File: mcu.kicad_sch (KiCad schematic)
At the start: 13 parts, among them J4 Conn_01x04, SW1 EVQ-P7A01P, SW2 EVQ-P7A01P, U2 TXB0304RUTR, U9 ESP32-S3-WROOM-1-N16R8

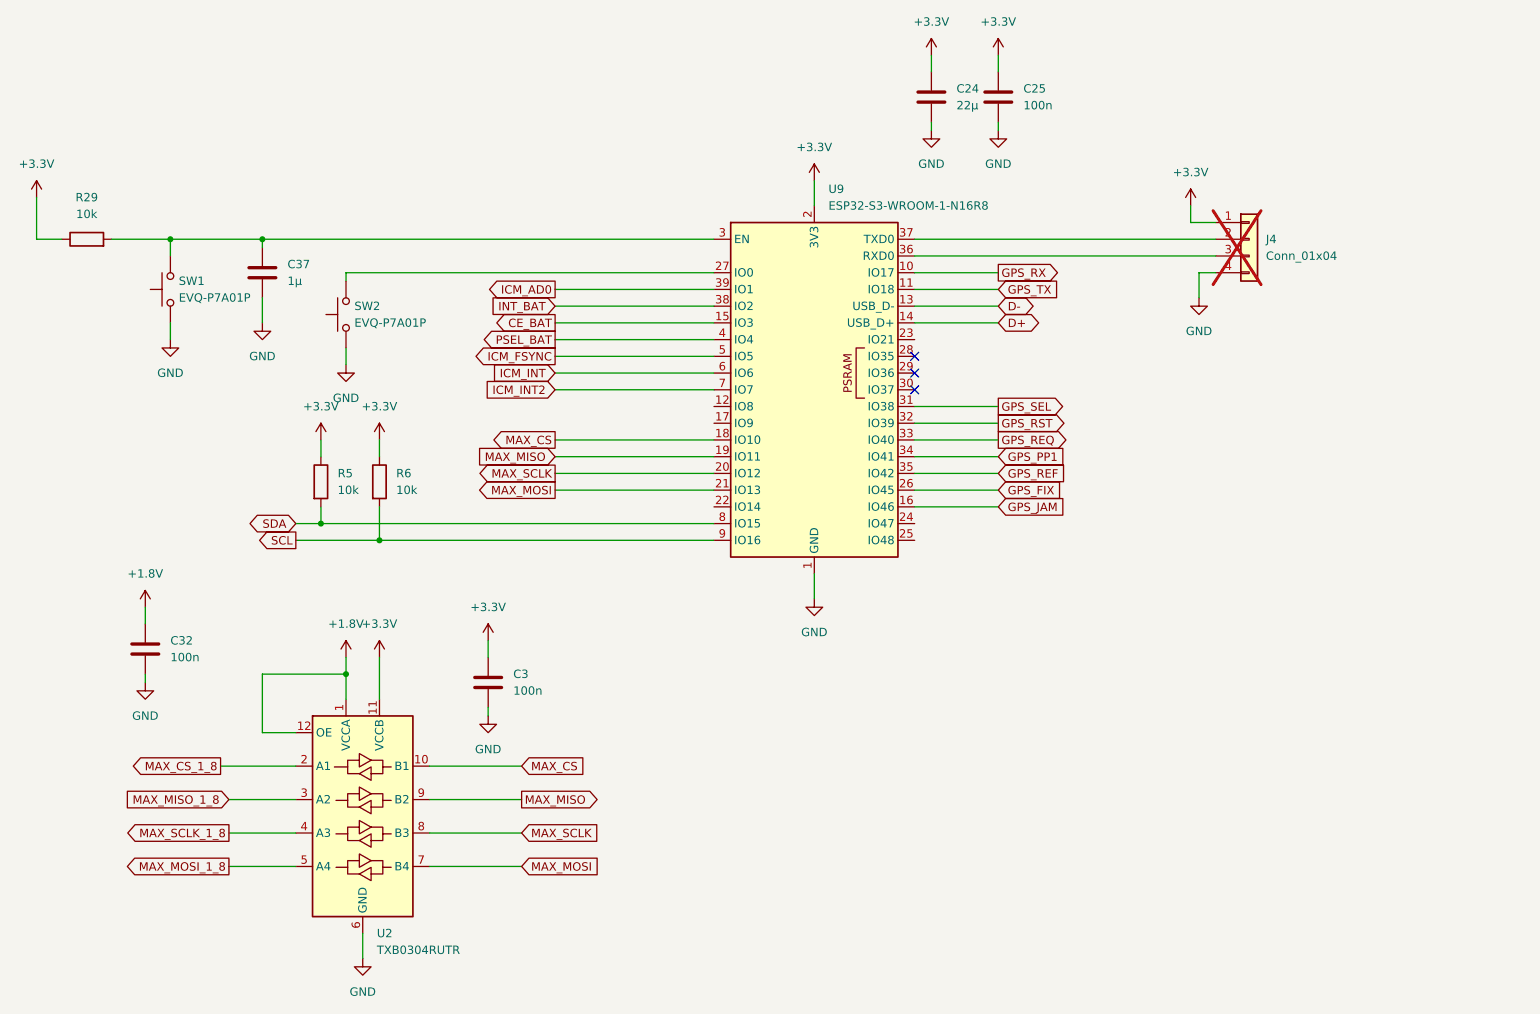
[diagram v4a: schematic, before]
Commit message: Add Flash device
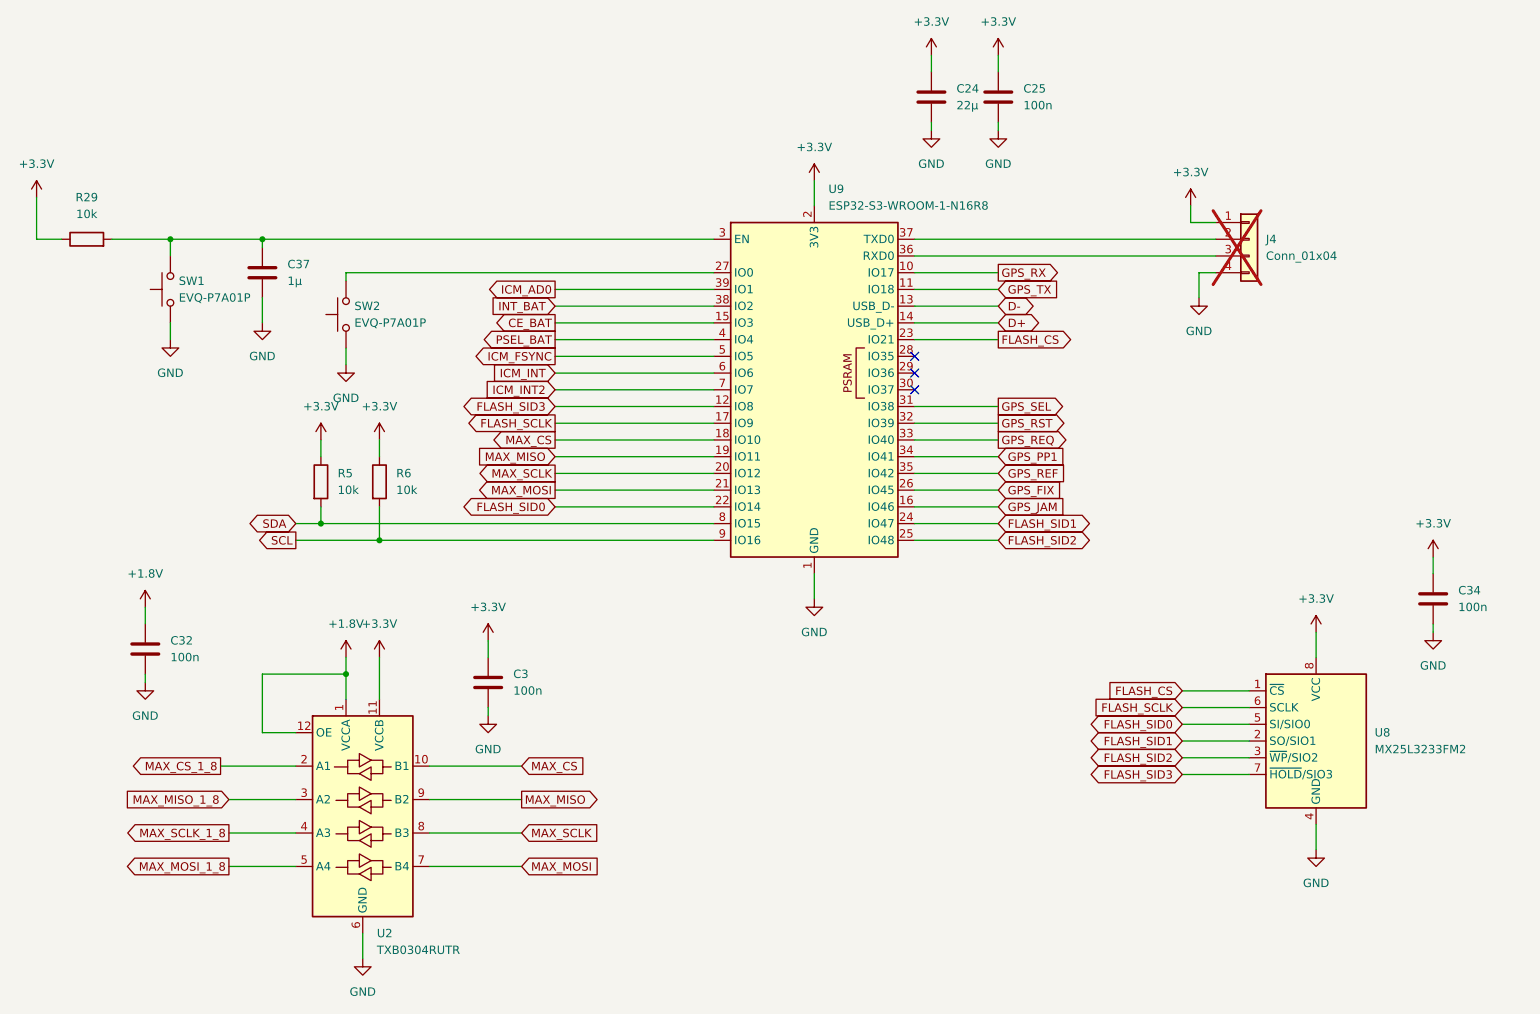
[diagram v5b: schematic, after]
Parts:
- added C34: 100n, Capacitor_SMD:C_0805_2012Metric, symbol Device:C
- added U8: MX25L3233FM2, Package_DFN_QFN:W-PDFN-8-1EP_6x5mm_P1.27mm_EP3x3mm, symbol Memory_Flash:MX25L3233FM2
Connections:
- net +3.3V: now also C34.1, U8.8 (VCC)
- net GND: now also C34.2, U8.4 (GND)
- net FLASH_SID3: now reaches U9.12 (IO8)
- net FLASH_SID3: now also U8.7 (~{HOLD}/SIO3)
- net FLASH_SCLK: now reaches U9.17 (IO9)
- net FLASH_SCLK: now also U8.6 (SCLK)
- net FLASH_SID0: now reaches U9.22 (IO14)
- net FLASH_SID0: now also U8.5 (SI/SIO0)
- net FLASH_CS: now reaches U9.23 (IO21)
- net FLASH_CS: now also U8.1 (~{CS})
- net FLASH_SID1: now reaches U9.24 (IO47)
- net FLASH_SID1: now also U8.2 (SO/SIO1)
- net FLASH_SID2: now reaches U9.25 (IO48)
- net FLASH_SID2: now also U8.3 (~{WP}/SIO2)

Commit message: Add version
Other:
- company: (none) -> Philippe12
- title: (none) -> HorseSense
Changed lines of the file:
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@@
 	(generator_version "9.0")
 	(paper "A4")
+	(title_block
+		(title "HorseSense")
+		(date "2025-11-01")
+		(rev "1.0")
+		(company "Philippe12")
+	)
 	(junction
 		(at 44.45 54.61)

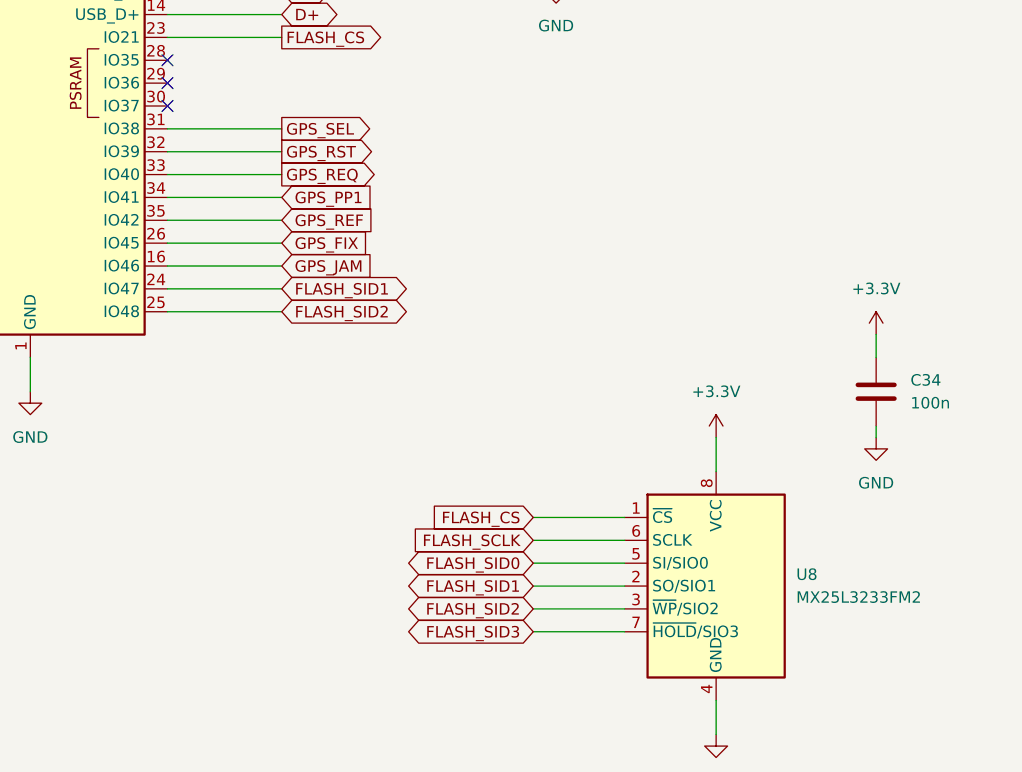
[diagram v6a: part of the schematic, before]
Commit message: Change GNSS device
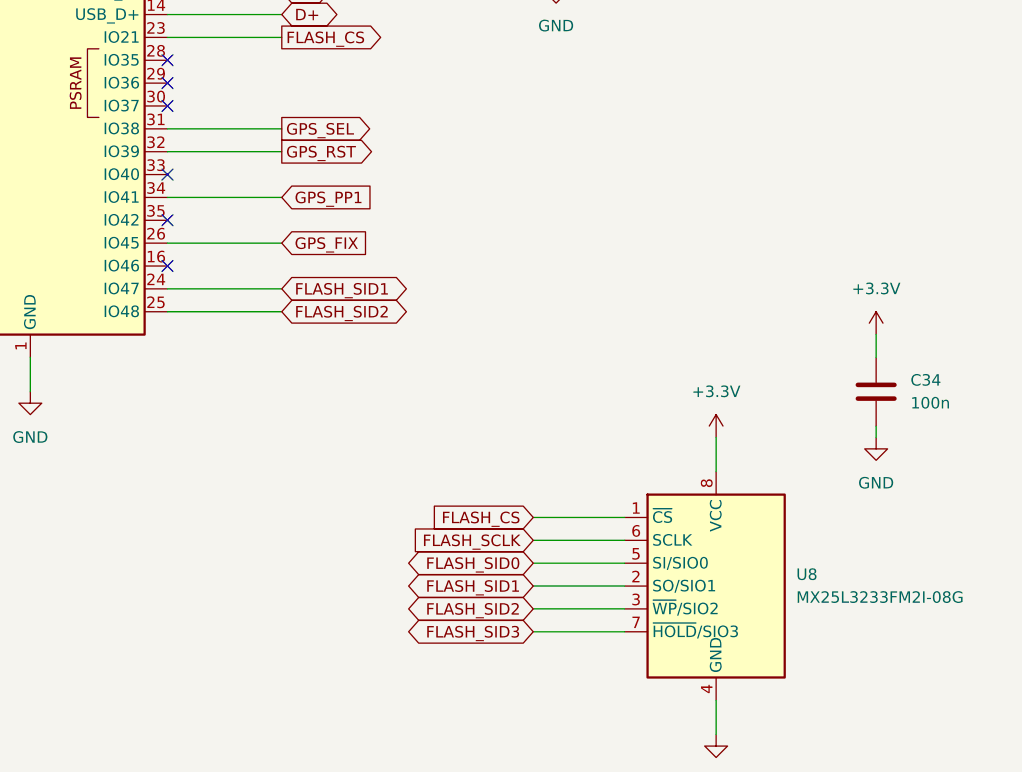
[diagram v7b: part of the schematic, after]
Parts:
- U8: value MX25L3233FM2 -> MX25L3233FM2I-08G; footprint Package_DFN_QFN:W-PDFN-8-1EP_6x5mm_P1.27mm_EP3x3mm -> Package_SO:SOIC-8_5.3x5.3mm_P1.27mm; JLCPCB Part # (none) -> C190802; manf# (none) -> MX25L3233FM2I-08G
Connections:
- net GPS_JAM: no longer names the net of U9.16 (IO46)
- net GPS_REF: no longer names the net of U9.35 (IO42)
- net GPS_REQ: no longer names the net of U9.33 (IO40)
- no-connect marks 3 -> 6

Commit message: Update for JLC parts
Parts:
- SW1: value EVQ-P7A01P -> EVQP7A01P; manf# EVQ-P7A01P -> EVQP7A01P
- SW2: value EVQ-P7A01P -> EVQP7A01P
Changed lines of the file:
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@@
 			)
 		)
-		(property "Sim.Enable" ""
+		(property "SnapEDA_Link" ""
 			(at 73.66 142.24 0)
 			(effects
@@
 			)
 		)
-		(property "SnapEDA_Link" ""
+		(property "Sim.Enable" ""
 			(at 73.66 142.24 0)
 			(effects
@@
 			)
 		)
-		(property "Value" "EVQ-P7A01P"
+		(property "Value" "EVQP7A01P"
 			(at 45.72 63.4999 90)
 			(effects
@@
 			)
 		)
-		(property "manf#" "EVQ-P7A01P"
+		(property "manf#" "EVQP7A01P"
 			(at 44.45 62.23 0)
 			(effects
@@
 			)
 		)
-		(property "Sim.Enable" ""
+		(property "SnapEDA_Link" ""
 			(at 44.45 62.23 90)
 			(effects
@@
 			)
 		)
-		(property "SnapEDA_Link" ""
+		(property "Sim.Enable" ""
 			(at 44.45 62.23 90)
 			(effects
@@
 			)
 		)
-		(property "Sim.Enable" ""
+		(property "SnapEDA_Link" ""
 			(at 76.2 91.44 0)
 			(effects
@@
 			)
 		)
-		(property "SnapEDA_Link" ""
+		(property "Sim.Enable" ""
 			(at 76.2 91.44 0)
 			(effects
@@
 			)
 		)
-		(property "Sim.Enable" ""
+		(property "SnapEDA_Link" ""
 			(at 31.75 54.61 90)
 			(effects
@@
 			)
 		)
-		(property "SnapEDA_Link" ""
+		(property "Sim.Enable" ""
 			(at 31.75 54.61 90)
 			(effects
@@
 			)
 		)
-		(property "Sim.Enable" ""
+		(property "SnapEDA_Link" ""
 			(at 218.44 130.81 0)
 			(effects
@@
 			)
 		)
-		(property "SnapEDA_Link" ""
+		(property "JLCPCB Part #" "C190802"
 			(at 218.44 130.81 0)
 			(effects
@@
 			)
 		)
-		(property "JLCPCB Part #" "C190802"
+		(property "manf#" "MX25L3233FM2I-08G"
 			(at 218.44 130.81 0)
 			(effects
@@
 			)
 		)
-		(property "manf#" "MX25L3233FM2I-08G"
+		(property "Sim.Enable" ""
 			(at 218.44 130.81 0)
 			(effects
@@
 			)
 		)
-		(property "Sim.Enable" ""
+		(property "SnapEDA_Link" ""
 			(at 142.24 77.47 0)
 			(effects
@@
 			)
 		)
-		(property "SnapEDA_Link" ""
+		(property "Sim.Enable" ""
 			(at 142.24 77.47 0)
 			(effects
@@
 			)
 		)
-		(property "Sim.Enable" ""
+		(property "SnapEDA_Link" ""
 			(at 208.28 54.61 0)
 			(effects
@@
 			)
 		)
-		(property "SnapEDA_Link" ""
+		(property "Sim.Enable" ""
 			(at 208.28 54.61 0)
 			(effects
@@
 			)
 		)
-		(property "Sim.Enable" ""
+		(property "SnapEDA_Link" ""
 			(at 67.31 91.44 0)
 			(effects
@@
 			)
 		)
-		(property "SnapEDA_Link" ""
+		(property "Sim.Enable" ""
 			(at 67.31 91.44 0)
 			(effects
@@
 			)
 		)
-		(property "Sim.Enable" ""
+		(property "SnapEDA_Link" ""
 			(at 92.71 121.92 0)
 			(effects
@@
 			)
 		)
-		(property "SnapEDA_Link" ""
+		(property "Sim.Enable" ""
 			(at 92.71 121.92 0)
 			(effects
@@
 			)
 		)
-		(property "Sim.Enable" ""
+		(property "SnapEDA_Link" ""
 			(at 170.18 33.02 0)
 			(effects
@@
 			)
 		)
-		(property "SnapEDA_Link" ""
+		(property "Sim.Enable" ""
 			(at 170.18 33.02 0)
 			(effects
@@
 			)
 		)
-		(property "Sim.Enable" ""
+		(property "SnapEDA_Link" ""
 			(at 40.64 116.84 0)
 			(effects
@@
 			)
 		)
-		(property "SnapEDA_Link" ""
+		(property "Sim.Enable" ""
 			(at 40.64 116.84 0)
 			(effects
@@
 			)
 		)
-		(property "Sim.Enable" ""
+		(property "SnapEDA_Link" ""
 			(at 58.42 59.69 0)
 			(effects
@@
 			)
 		)
-		(property "SnapEDA_Link" ""
+		(property "Sim.Enable" ""
 			(at 58.42 59.69 0)
 			(effects
@@
 			)
 		)
-		(property "Value" "EVQ-P7A01P"
+		(property "Value" "EVQP7A01P"
 			(at 72.39 67.3099 90)
 			(effects
@@
 			)
 		)
-		(property "Sim.Enable" ""
+		(property "SnapEDA_Link" ""
 			(at 71.12 66.04 90)
 			(effects
@@
 			)
 		)
-		(property "SnapEDA_Link" ""
+		(property "Sim.Enable" ""
 			(at 71.12 66.04 90)
 			(effects
@@
 			)
 		)
-		(property "Sim.Enable" ""
+		(property "SnapEDA_Link" ""
 			(at 236.22 109.22 0)
 			(effects
@@
 			)
 		)
-		(property "SnapEDA_Link" ""
+		(property "Sim.Enable" ""
 			(at 236.22 109.22 0)
 			(effects
@@
 			)
 		)
-		(property "Sim.Enable" ""
+		(property "SnapEDA_Link" ""
 			(at 160.02 33.02 0)
 			(effects
@@
 			)
 		)
-		(property "SnapEDA_Link" ""
+		(property "Sim.Enable" ""
 			(at 160.02 33.02 0)
 			(effects
